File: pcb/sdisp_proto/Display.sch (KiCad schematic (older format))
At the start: 15 parts, among them P1 CONN_02X05, U1 74HC595

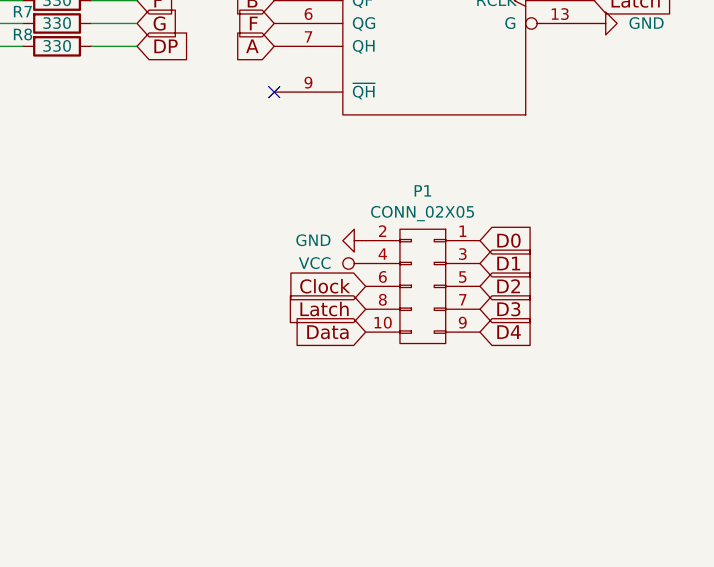
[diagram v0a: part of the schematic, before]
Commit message: Fix: Layout of the pin header on the prototype
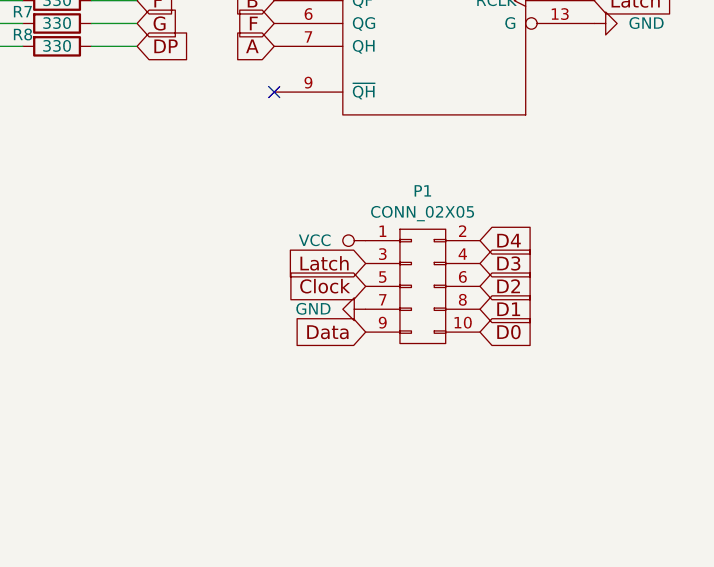
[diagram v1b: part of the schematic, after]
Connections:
- net Clock: now also P1.5 (P5); no longer P1.6 (P6)
- net D0: now also P1.10 (P10); no longer P1.1 (P1)
- net D1: now also P1.8 (P8); no longer P1.3 (P3)
- net D2: now also P1.6 (P6); no longer P1.5 (P5)
- net D3: now also P1.4 (P4); no longer P1.7 (P7)
- net D4: now also P1.2 (P2); no longer P1.9 (P9)
- net Data: now also P1.9 (P9); no longer P1.10 (P10)
- net GND: now also P1.7 (P7); no longer P1.2 (P2)
- net Latch: now also P1.3 (P3); no longer P1.8 (P8)
- net VCC: now also P1.1 (P1); no longer P1.4 (P4)
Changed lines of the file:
@@
 F 3 "" H 5250 1450 50  0000 C CNN
 	1    5250 2650
-	-1   0    0    -1
+	1    0    0    -1
 $EndComp
 NoConn ~ 4600 1800
@@
 	0    1    -1   0
 $EndComp
-Text GLabel 5500 2450 2    60   Input ~ 0
+Text GLabel 5500 2850 2    60   Input ~ 0
 D0
-Text GLabel 5500 2550 2    60   Input ~ 0
+Text GLabel 5500 2750 2    60   Input ~ 0
 D1
 Text GLabel 5500 2650 2    60   Input ~ 0
 D2
-Text GLabel 5500 2750 2    60   Input ~ 0
+Text GLabel 5500 2550 2    60   Input ~ 0
 D3
-Text GLabel 5500 2850 2    60   Input ~ 0
+Text GLabel 5500 2450 2    60   Input ~ 0
 D4
 $Comp
 L VCC #PWR02
 U 1 1 5678FB4C
-P 5000 2550
-F 0 "#PWR02" H 5000 2400 50  0001 C CNN
-F 1 "VCC" V 5000 2700 50  0000 L CNN
-F 2 "" H 5000 2550 50  0000 C CNN
-F 3 "" H 5000 2550 50  0000 C CNN
-	1    5000 2550
+P 5000 2450
+F 0 "#PWR02" H 5000 2300 50  0001 C CNN
+F 1 "VCC" V 5000 2600 50  0000 L CNN
+F 2 "" H 5000 2450 50  0000 C CNN
+F 3 "" H 5000 2450 50  0000 C CNN
+	1    5000 2450
 	0    -1   -1   0
 $EndComp
@@
 L GND #PWR03
 U 1 1 5678FB77
-P 5000 2450
-F 0 "#PWR03" H 5000 2200 50  0001 C CNN
-F 1 "GND" V 5000 2300 50  0000 R CNN
-F 2 "" H 5000 2450 50  0000 C CNN
-F 3 "" H 5000 2450 50  0000 C CNN
-	1    5000 2450
+P 5000 2750
+F 0 "#PWR03" H 5000 2500 50  0001 C CNN
+F 1 "GND" V 5000 2600 50  0000 R CNN
+F 2 "" H 5000 2750 50  0000 C CNN
+F 3 "" H 5000 2750 50  0000 C CNN
+	1    5000 2750
 	0    1    1    0
 $EndComp
@@
 Text GLabel 5000 2650 0    60   Input ~ 0
 Clock
-Text GLabel 5000 2750 0    60   Input ~ 0
+Text GLabel 5000 2550 0    60   Input ~ 0
 Latch
 Text GLabel 4000 900  2    60   Input ~ 0
